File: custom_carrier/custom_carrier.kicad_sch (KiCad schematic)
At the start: 2 parts, among them J1 ERF5-040-05.0-X-DV, J2 ERF5-040-05.0-X-DV

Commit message: working on custom carrier in V7
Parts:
- added J3: PJ-002AH-SMT-TR, pedrolib:CUI_PJ-002AH-SMT-TR, symbol pedrolib:PJ-002AH-SMT-TR
- added J4: 87832-1420, pedrolib:MOLEX_87832-1420, symbol pedrolib:87832-1420
- added J5, J6: ERF5-040-05.0-X-DV, pedrolib:SAMTEC_ERF5-040-05.0-X-DV, symbol pedrolib:ERF5-040-05.0-X-DV
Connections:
- new net: J3.1A, J3.1B
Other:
- moved on the sheet: J1, J2

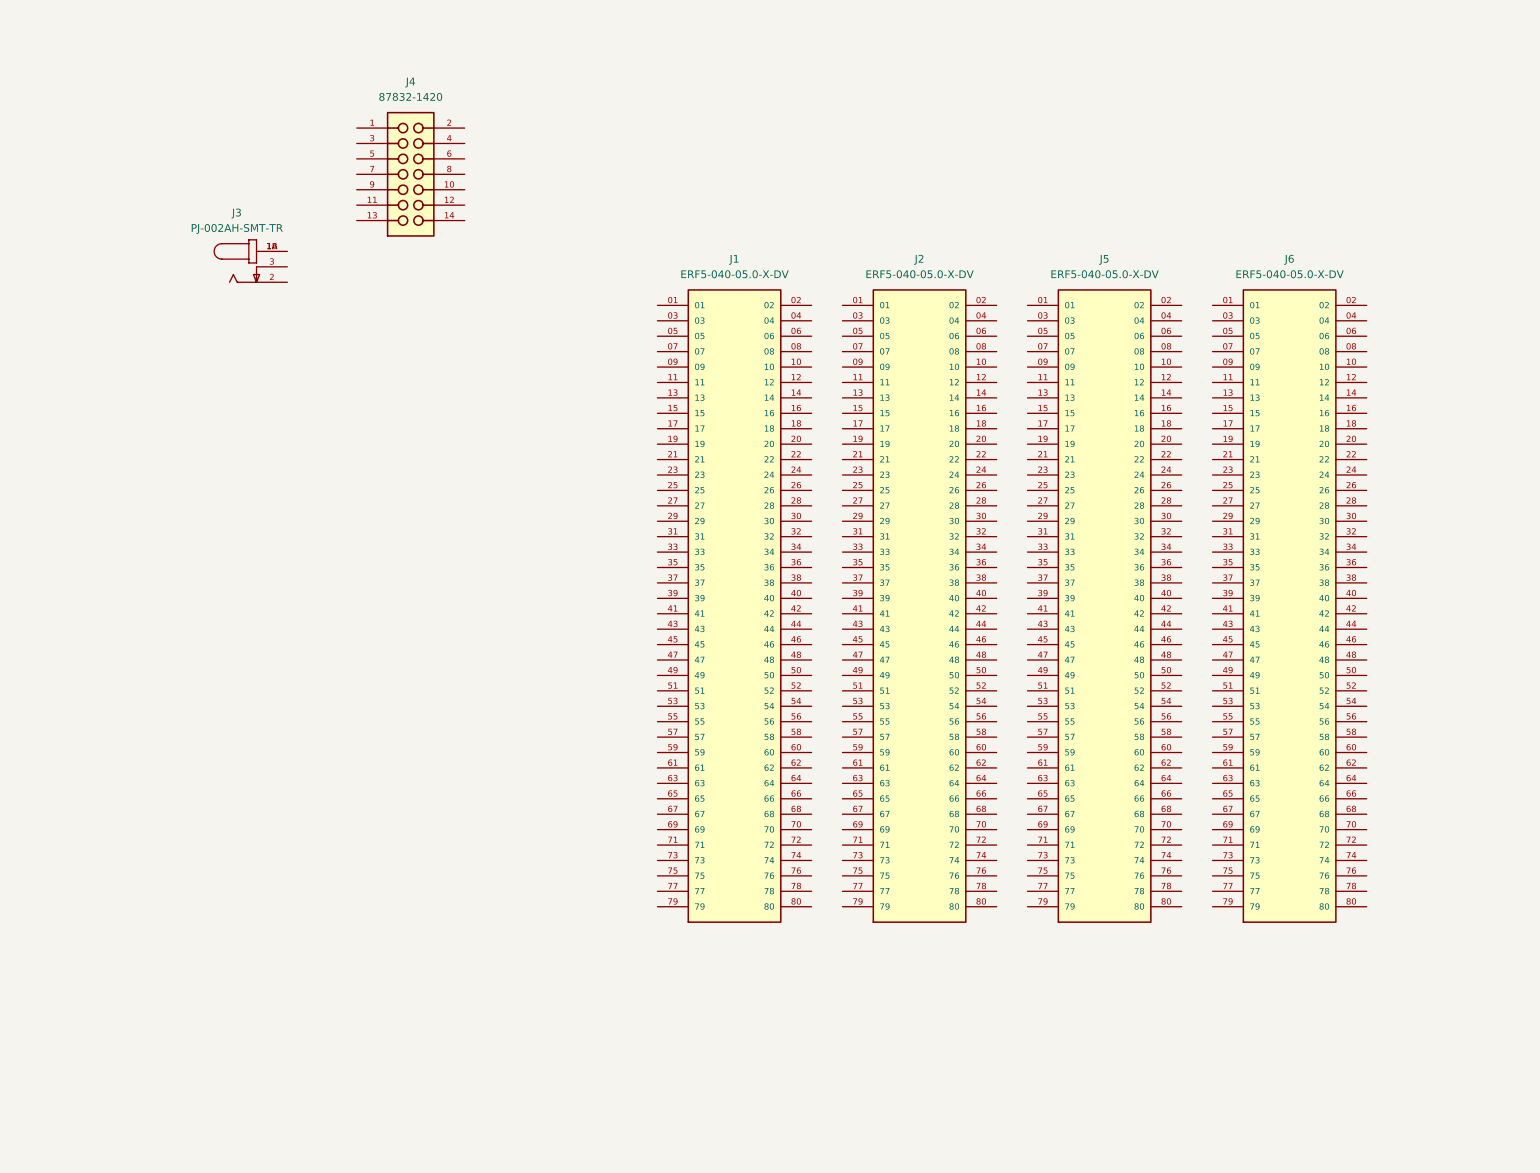
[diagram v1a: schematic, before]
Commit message: added ribbon cable connectors
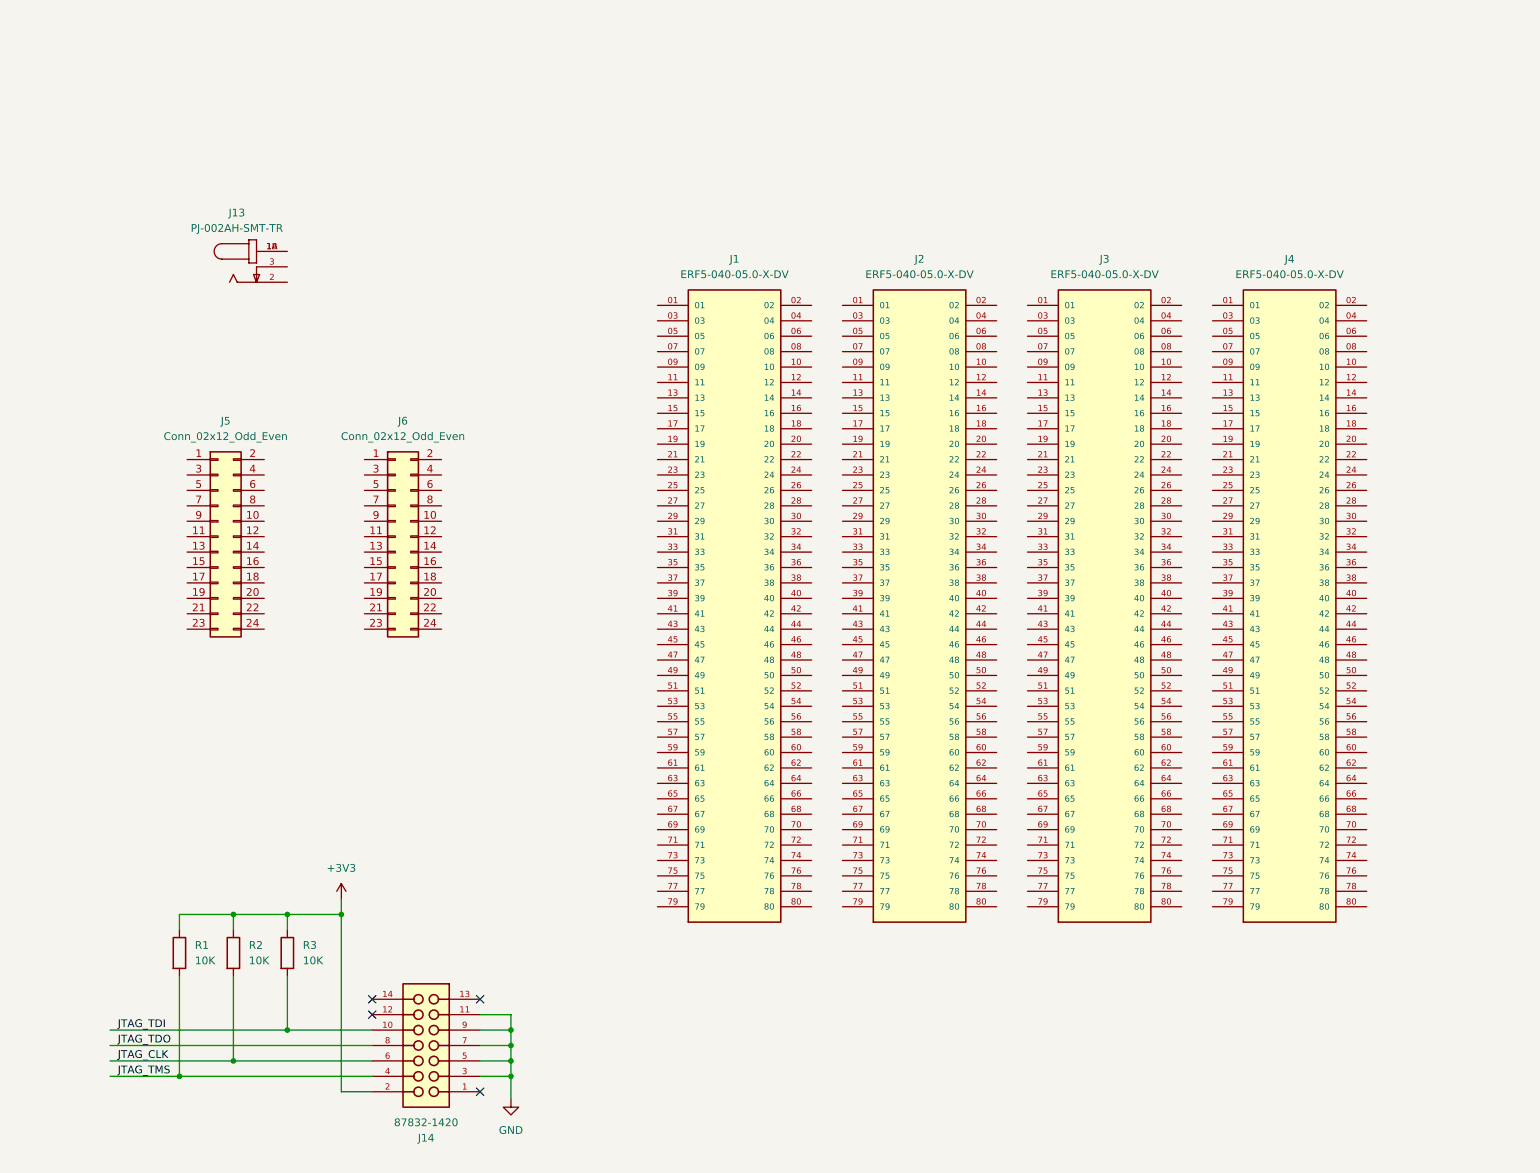
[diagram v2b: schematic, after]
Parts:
- added J5, J6: Conn_02x12_Odd_Even, Connector_PinHeader_2.54mm:PinHeader_2x12_P2.54mm_Vertical, symbol Connector_Generic:Conn_02x12_Odd_Even
- added R1, R2, R3: 10K, Resistor_SMD:R_0603_1608Metric, symbol Device:R
- renumbered J3 to J13, J4 to J14, J5 to J3, J6 to J4
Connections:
- net JTAG_TDI: now reaches J14.10
- net JTAG_TDI: now also R3.2
- net GND: now reaches J14.11
- net GND: now also J14.3, J14.5, J14.7, J14.9
- net +3V3: now reaches J14.2
- net +3V3: now also R1.1, R2.1, R3.1
- net JTAG_TMS: now reaches J14.4
- net JTAG_TMS: now also R1.2
- net JTAG_CLK: now reaches J14.6
- net JTAG_CLK: now also R2.2
- net JTAG_TDO: now reaches J14.8
- no-connect marks 0 -> 4
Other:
- moved on the sheet: J14

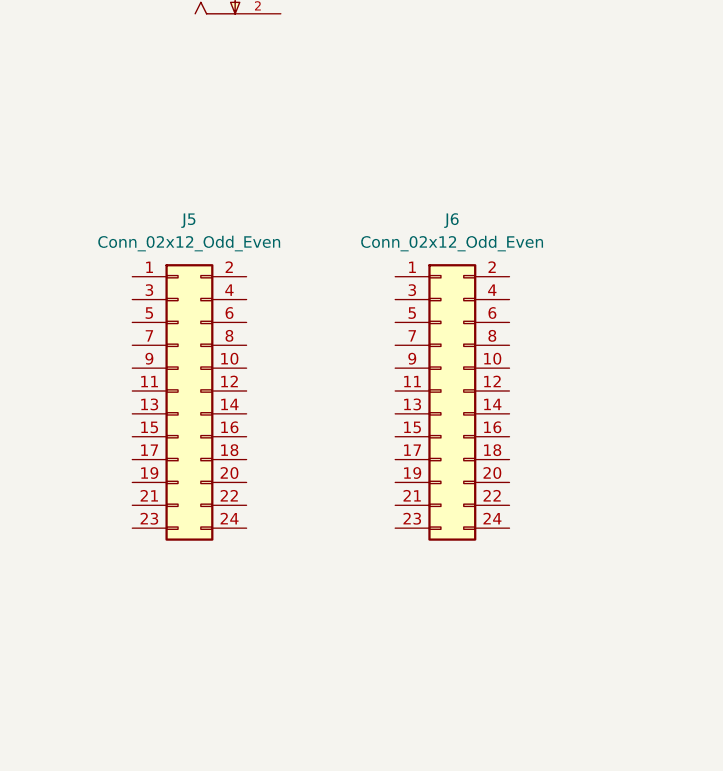
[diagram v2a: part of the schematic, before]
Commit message: added 3M connector
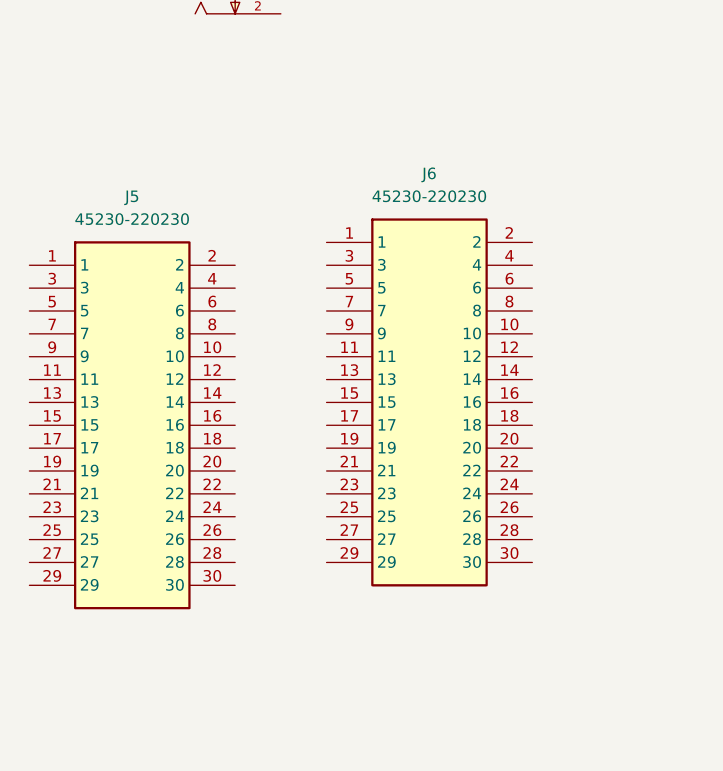
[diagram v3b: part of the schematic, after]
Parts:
- removed J5, J6: Conn_02x12_Odd_Even, Connector_PinHeader_2.54mm:PinHeader_2x12_P2.54mm_Vertical, symbol Connector_Generic:Conn_02x12_Odd_Even
- added J5, J6: 45230-220230, pedrolib:45230220230, symbol pedrolib:45230-220230
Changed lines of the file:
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@@
-    )
-  )
-  (symbol (lib_id "Connector_Generic:Conn_02x12_Odd_Even") (at 48.26 99.06 0) (unit 1)
-    (in_bom yes) (on_board yes) (dnp no) (fields_autoplaced)
-    (property "Reference" "J5" (at 49.53 80.01 0)
-      (effects (font (size 1.27 1.27)))
-    )
-    (property "Value" "Conn_02x12_Odd_Even" (at 49.53 82.55 0)
-      (effects (font (size 1.27 1.27)))
-    )
-    (property "Footprint" "Connector_PinHeader_2.54mm:PinHeader_2x12_P2.54mm_Vertical" (at 48.26 99.06 0)
-      (effects (font (size 1.27 1.27)) hide)
-    )
-    (property "Datasheet" "~" (at 48.26 99.06 0)
-      (effects (font (size 1.27 1.27)) hide)
-    )
-    (pin "2")
-    (pin "24")
-    (pin "6")
-    (pin "5")
-    (pin "3")
-    (pin "4")
-    (pin "23")
-    (pin "21")
-    (pin "15")
-    (pin "1")
-    (pin "18")
-    (pin "8")
-    (pin "20")
-    (pin "9")
-    (pin "17")
-    (pin "14")
-    (pin "11")
-    (pin "7")
-    (pin "13")
-    (pin "12")
-    (pin "19")
-    (pin "10")
-    (pin "16")
-    (pin "22")
-    (instances
-      (project "custom_carrier"
-        (path "/36e0264f-a69b-47b3-a9ec-651b758a8d35"
-          (reference "J5") (unit 1)
-        )
-      )
     )
   )
@@
     )
   )
+  (symbol (lib_id "pedrolib:45230-220230") (at 64.77 82.55 0) (unit 1)
+    (in_bom yes) (on_board yes) (dnp no) (fields_autoplaced)
+    (property "Reference" "J6" (at 76.2 74.93 0)
+      (effects (font (size 1.27 1.27)))
+    )
+    (property "Value" "45230-220230" (at 76.2 77.47 0)
+      (effects (font (size 1.27 1.27)))
+    )
+    (property "Footprint" "pedrolib:45230220230" (at 83.82 177.47 0)
+      (effects (font (size 1.27 1.27)) (justify left top) hide)
+    )
+    (property "Datasheet" "https://multimedia.3m.com/mws/media/905148O/3m-shrouded-boardmount-header-452-series-cd2437.pdf" (at 83.82 277.47 0)
+      (effects (font (size 1.27 1.27)) (justify left top) hide)
+    )
+    (property "Height" "5.893" (at 83.82 477.47 0)
+      (effects (font (size 1.27 1.27)) (justify left top) hide)
+    )
+    (property "Manufacturer_Name" "3M" (at 83.82 577.47 0)
+      (effects (font (size 1.27 1.27)) (justify left top) hide)
+    )
+    (property "Manufacturer_Part_Number" "45230-220230" (at 83.82 677.47 0)
+      (effects (font (size 1.27 1.27)) (justify left top) hide)
+    )
+    (property "Mouser Part Number" "517-45230-220230" (at 83.82 777.47 0)
+      (effects (font (size 1.27 1.27)) (justify left top) hide)
+    )
+    (property "Mouser Price/Stock" "https://www.mouser.co.uk/ProductDetail/3M-Electronic-Solutions-Division/45230-220230?qs=sowatxGsQyy8V6SB6XJn%2FA%3D%3D" (at 83.82 877.47 0)
+      (effects (font (size 1.27 1.27)) (justify left top) hide)
+    )
+    (property "Arrow Part Number" "45230-220230" (at 83.82 977.47 0)
+      (effects (font (size 1.27 1.27)) (justify left top) hide)
+    )
+    (property "Arrow Price/Stock" "https://www.arrow.com/en/products/45230-220230/3m?region=nac" (at 83.82 1077.47 0)
+      (effects (font (size 1.27 1.27)) (justify left top) hide)
+    )
+    (pin "1")
+    (pin "3")
+    (pin "4")
+    (pin "10")
+    (pin "8")
+    (pin "27")
+    (pin "9")
+    (pin "22")
+    (pin "14")
+    (pin "13")
+    (pin "2")
+    (pin "19")
+    (pin "12")
+    (pin "30")
+    (pin "20")
+    (pin "6")
+    (pin "5")
+    (pin "21")
+    (pin "28")
+    (pin "11")
+    (pin "18")
+    (pin "7")
+    (pin "29")
+    (pin "26")
+    (pin "25")
+    (pin "23")
+    (pin "17")
+    (pin "16")
+    (pin "24")
+    (pin "15")
+    (instances
+      (project "custom_carrier"
+        (path "/36e0264f-a69b-47b3-a9ec-651b758a8d35"
+          (reference "J6") (unit 1)
+        )
+      )
+    )
+  )
+  (symbol (lib_id "pedrolib:45230-220230") (at 31.75 85.09 0) (unit 1)
+    (in_bom yes) (on_board yes) (dnp no) (fields_autoplaced)
+    (property "Reference" "J5" (at 43.18 77.47 0)
+      (effects (font (size 1.27 1.27)))
+    )
+    (property "Value" "45230-220230" (at 43.18 80.01 0)
+      (effects (font (size 1.27 1.27)))
+    )
+    (property "Footprint" "pedrolib:45230220230" (at 50.8 180.01 0)
+      (effects (font (size 1.27 1.27)) (justify left top) hide)
+    )
+    (property "Datasheet" "https://multimedia.3m.com/mws/media/905148O/3m-shrouded-boardmount-header-452-series-cd2437.pdf" (at 50.8 280.01 0)
+      (effects (font (size 1.27 1.27)) (justify left top) hide)
+    )
+    (property "Height" "5.893" (at 50.8 480.01 0)
+      (effects (font (size 1.27 1.27)) (justify left top) hide)
+    )
+    (property "Manufacturer_Name" "3M" (at 50.8 580.01 0)
+      (effects (font (size 1.27 1.27)) (justify left top) hide)
+    )
+    (property "Manufacturer_Part_Number" "45230-220230" (at 50.8 680.01 0)
+      (effects (font (size 1.27 1.27)) (justify left top) hide)
+    )
+    (property "Mouser Part Number" "517-45230-220230" (at 50.8 780.01 0)
+      (effects (font (size 1.27 1.27)) (justify left top) hide)
+    )
+    (property "Mouser Price/Stock" "https://www.mouser.co.uk/ProductDetail/3M-Electronic-Solutions-Division/45230-220230?qs=sowatxGsQyy8V6SB6XJn%2FA%3D%3D" (at 50.8 880.01 0)
+      (effects (font (size 1.27 1.27)) (justify left top) hide)
+    )
+    (property "Arrow Part Number" "45230-220230" (at 50.8 980.01 0)
+      (effects (font (size 1.27 1.27)) (justify left top) hide)
+    )
+    (property "Arrow Price/Stock" "https://www.arrow.com/en/products/45230-220230/3m?region=nac" (at 50.8 1080.01 0)
+      (effects (font (size 1.27 1.27)) (justify left top) hide)
+    )
+    (pin "28")
+    (pin "21")
+    (pin "19")
+    (pin "6")
+    (pin "20")
+    (pin "18")
+    (pin "15")
+    (pin "30")
+    (pin "2")
+    (pin "9")
+    (pin "5")
+    (pin "22")
+    (pin "10")
+    (pin "4")
+    (pin "11")
+    (pin "12")
+    (pin "1")
+    (pin "24")
+    (pin "29")
+    (pin "27")
+    (pin "25")
+    (pin "23")
+    (pin "26")
+    (pin "13")
+    (pin "3")
+    (pin "14")
+    (pin "17")
+    (pin "8")
+    (pin "7")
+    (pin "16")
+    (instances
+      (project "custom_carrier"
+        (path "/36e0264f-a69b-47b3-a9ec-651b758a8d35"
+          (reference "J5") (unit 1)
+        )
+      )
+    )
+  )
   (symbol (lib_id "pedrolib:ERF5-040-05.0-X-DV") (at 163.83 109.22 0) (unit 1)
     (in_bom yes) (on_board yes) (dnp no) (fields_autoplaced)
@@
         )
       )
-    )
-  )
-  (symbol (lib_id "Connector_Generic:Conn_02x12_Odd_Even") (at 77.47 99.06 0) (unit 1)
-    (in_bom yes) (on_board yes) (dnp no) (fields_autoplaced)
-    (property "Reference" "J6" (at 78.74 80.01 0)
-      (effects (font (size 1.27 1.27)))
-    )
-    (property "Value" "Conn_02x12_Odd_Even" (at 78.74 82.55 0)
-      (effects (font (size 1.27 1.27)))
-    )
-    (property "Footprint" "Connector_PinHeader_2.54mm:PinHeader_2x12_P2.54mm_Vertical" (at 77.47 99.06 0)
-      (effects (font (size 1.27 1.27)) hide)
-    )
-    (property "Datasheet" "~" (at 77.47 99.06 0)
-      (effects (font (size 1.27 1.27)) hide)
-    )
-    (pin "2")
-    (pin "24")
-    (pin "6")
-    (pin "5")
-    (pin "3")
-    (pin "4")
-    (pin "23")
-    (pin "21")
-    (pin "15")
-    (pin "1")
-    (pin "18")
-    (pin "8")
-    (pin "20")
-    (pin "9")
-    (pin "17")
-    (pin "14")
-    (pin "11")
-    (pin "7")
-    (pin "13")
-    (pin "12")
-    (pin "19")
-    (pin "10")
-    (pin "16")
-    (pin "22")
-    (instances
-      (project "custom_carrier"
-        (path "/36e0264f-a69b-47b3-a9ec-651b758a8d35"
-          (reference "J6") (unit 1)
-        )
-      )

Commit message: working on high-speed cables.
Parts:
- added C1: 22UF/25V, Capacitor_Tantalum_SMD:CP_EIA-3528-15_AVX-H, symbol Device:C_Polarized_Small
- added H1, H2, H3, H4: standoff_hole, MountingHole:MountingHole_2.2mm_M2_DIN965_Pad, symbol pedrolib:standoff_hole
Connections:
- net +3V3: now also J1.75, J1.76, J2.75, J2.76
- net GND: now also J1.01, J1.02, J1.11, J1.12, J1.21, J1.22, J1.31, J1.32, J1.41, J1.42, J1.51, J1.52, J1.61, J1.62, J1.70, J1.73, J1.74, J1.79, J1.80, J13.2, J13.3, J2.01, J2.02, J2.11, J2.12, J2.21, J2.22, J2.31, J2.32, J2.41, J2.42, J2.51, J2.52, J2.61, J2.62, J2.73, J2.74, J2.79, J2.80, J3.01, J3.02, J3.07, J3.08, J3.13, J3.14, J3.19, J3.20, J3.25, J3.26, J3.31, J3.32, J3.37, J3.38, J3.43, J3.44, J3.49, J3.50, J3.55, J3.56, J3.61, J3.62, J3.67, J3.68, J3.73, J3.74, J3.79, J3.80, J4.01, J4.02, J4.07, J4.08, J4.13, J4.14, J4.19, J4.20, J4.25, J4.26, J4.31, J4.32, J4.37, J4.38, J4.43, J4.44, J4.49, J4.50, J4.55, J4.56, J4.61, J4.62, J4.67, J4.68, J4.73, J4.74, J4.79, J4.80, J5.1, J5.11, J5.13, J5.15, J5.17, J5.19, J5.21, J5.23, J5.25, J5.27, J5.29, J5.3, J5.30, J5.5, J5.7, J5.9, J6.1, J6.11, J6.13, J6.15, J6.17, J6.19, J6.21, J6.23, J6.25, J6.27, J6.29, J6.3, J6.30, J6.5, J6.7, J6.9, C1.2, H1.1, H2.1, H3.1, H4.1
- net JTAG_CLK: now also J2.67
- net JTAG_TDI: now also J2.63
- net JTAG_TDO: now also J2.65
- net JTAG_TMS: now also J2.69
- net +12V: now reaches J13.1A, J13.1B
- net +12V: now also J1.64, J1.66, J1.68, C1.1
- net CH1_RX3_P: now reaches J4.10
- net CH1_RX3_P: now also J5.20
- net CH1_RX3_N: now reaches J4.12
- net CH1_RX3_N: now also J5.18
- net CH1_RX2_P: now reaches J4.16
- net CH1_RX2_P: now also J5.16
- net CH1_RX2_N: now reaches J4.18
- net CH1_RX2_N: now also J5.14
- net CH0_DCO_P: now reaches J4.21
- net CH0_DCO_P: now also J4.51
- net CH1_RX1_P: now reaches J4.22
- net CH1_RX1_P: now also J5.12
- net CH0_DCO_N: now reaches J4.23
- net CH0_DCO_N: now also J4.53
- net CH1_RX1_N: now reaches J4.24
- net CH1_RX1_N: now also J5.10
- net CH0_D3_P: now reaches J4.27
- net CH0_D3_P: now also J4.57
- net CH1_RX0_P: now reaches J4.28
- net CH1_RX0_P: now also J5.8
- net CH0_D3_N: now reaches J4.29
- net CH0_D3_N: now also J4.59
- net CH1_RX0_N: now reaches J4.30
- net CH1_RX0_N: now also J5.6
- net CH0_D2_P: now reaches J4.33
- net CH0_D2_P: now also J4.63
- net CH1_DCO_P: now reaches J4.34
- net CH1_DCO_P: now also J5.4
- net CH0_D2_N: now reaches J4.35
- net CH0_D2_N: now also J4.65
- net CH1_DCO_N: now reaches J4.36
- net CH1_DCO_N: now also J5.2
- net CH0_D1_P: now reaches J4.39
- net CH0_D1_P: now also J4.69
- net CH1_TX3_P: now reaches J4.40
- net CH1_TX3_P: now also J6.20
- net CH0_D1_N: now reaches J4.41
- net CH0_D1_N: now also J4.71
- net CH1_TX3_N: now reaches J4.42
- net CH1_TX3_N: now also J6.18
- net CH0_D0_P: now reaches J4.45
- net CH0_D0_P: now also J4.75
- net CH1_TX2_P: now reaches J4.46
- net CH1_TX2_P: now also J6.16
- net CH0_D0_N: now reaches J4.47
- net CH0_D0_N: now also J4.77
- net CH1_TX2_N: now reaches J4.48
- net CH1_TX2_N: now also J6.14
- net CH1_TX1_P: now reaches J4.52
- net CH1_TX1_P: now also J6.12
- net CH1_TX1_N: now reaches J4.54
- net CH1_TX1_N: now also J6.10
- net CH1_TX0_P: now reaches J4.58
- net CH1_TX0_P: now also J6.8
- net CH1_TX0_N: now reaches J4.60
- net CH1_TX0_N: now also J6.6
- net CH1_CLK_P: now reaches J4.64
- net CH1_CLK_P: now also J6.4
- net CH1_CLK_N: now reaches J4.66
- net CH1_CLK_N: now also J6.2
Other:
- title: (none) -> Custom Carrier
- moved on the sheet: J1, J13, J14, J2, J3, J4, J5, J6, R1, R2, R3
